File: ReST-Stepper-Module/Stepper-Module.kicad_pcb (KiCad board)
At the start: 2 copper layers, 46 x 32.8 mm, 16 parts, among them P1 CONN_02X10, P2 CONN_01X04, P3 CONN_01X04, P4 CONN_01X04, P5 CONN_01X04, P6 CONN_02X03, P7 CONN_02X03, U1 POLOLU_A4988, U2 POLOLU_A4988

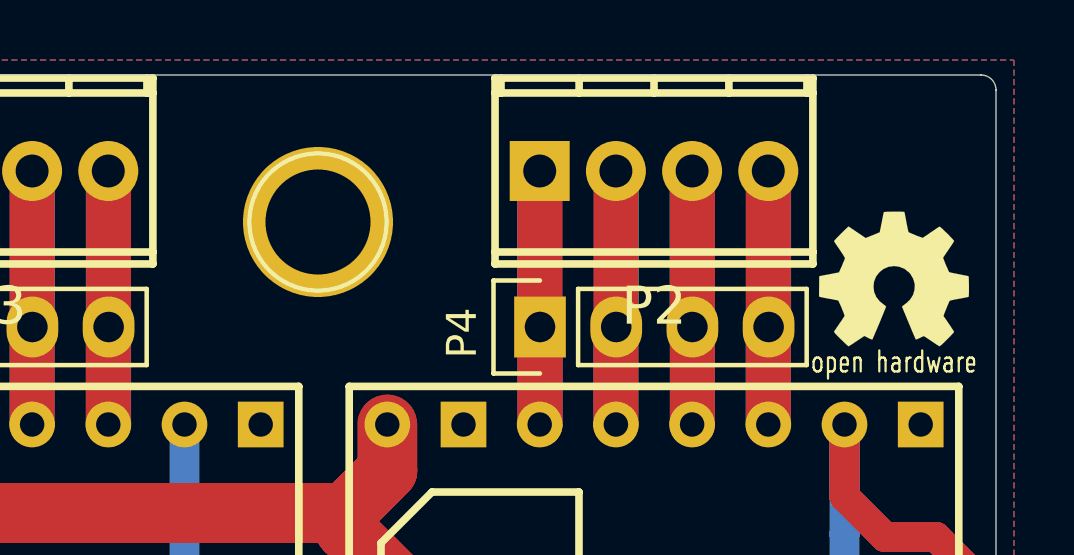
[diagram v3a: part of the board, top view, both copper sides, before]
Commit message: Added IRLML2502 Module and added Ground vias everywhere
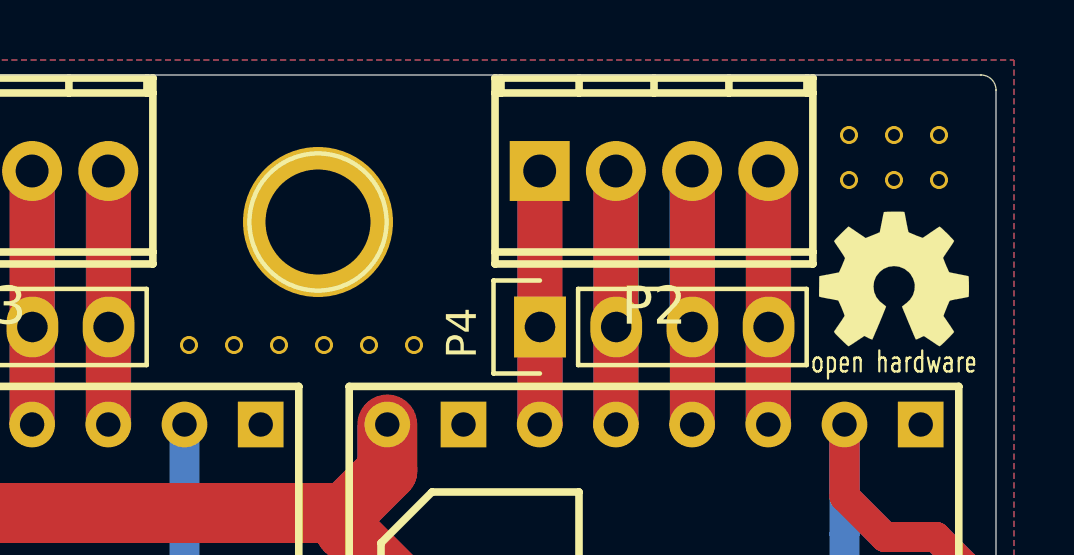
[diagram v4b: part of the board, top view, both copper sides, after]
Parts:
- added 11: , ReST-Library:VIA-0.6mm, F.Cu at (121.5, 87.0)
- added 21: , ReST-Library:VIA-0.6mm, F.Cu at (123.0, 87.0)
- added 31: , ReST-Library:VIA-0.6mm, F.Cu at (124.5, 87.0)
- added 41: , ReST-Library:VIA-0.6mm, F.Cu at (126.0, 87.0)
- added 51: , ReST-Library:VIA-0.6mm, F.Cu at (127.5, 87.0)
- added 61: , ReST-Library:VIA-0.6mm, F.Cu at (129.0, 87.0)
- added 611: , ReST-Library:VIA-0.6mm, F.Cu at (143.5, 80.0)
- added 612: , ReST-Library:VIA-0.6mm, F.Cu at (143.5, 81.5)
- added 621: , ReST-Library:VIA-0.6mm, F.Cu at (145.0, 80.0)
- added 622: , ReST-Library:VIA-0.6mm, F.Cu at (145.0, 81.5)
- added 631: , ReST-Library:VIA-0.6mm, F.Cu at (146.5, 80.0)
- added 632: , ReST-Library:VIA-0.6mm, F.Cu at (146.5, 81.5)
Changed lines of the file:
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@@
 (kicad_pcb (version 4) (host pcbnew 4.0.1-stable)
   (general
-    (links 63)
+    (links 75)
     (no_connects 0)
-    (area 84 59.2 165.800001 128.400001)
+    (area 102.394999 77.994999 148.405001 110.805001)
     (thickness 1.6)
     (drawings 9)
     (tracks 205)
     (zones 0)
-    (modules 16)
+    (modules 28)
     (nets 26)
   )
@@
     (mod_text_size 1 1)
     (mod_text_width 0.15)
-    (pad_size 5 5)
-    (pad_drill 3.5)
+    (pad_size 0.6 0.6)
+    (pad_drill 0.4)
     (pad_to_mask_clearance 0.2)
     (aux_axis_origin 0 0)
@@
     (add_net "Net-(U1-Pad13)")
     (add_net "Net-(U2-Pad13)")
+  )
+  (module ReST-Library:VIA-0.6mm (layer F.Cu)
+    (at 146.5 81.5)
+    (fp_text reference 632 (at 0 3.5) (layer F.SilkS) hide
+      (effects (font (size 1 1) (thickness 0.15)))
+    )
+    (fp_text value "" (at 0 -3) (layer F.Fab) hide
+      (effects (font (size 1 1) (thickness 0.15)))
+    )
+    (pad 2 thru_hole circle (at 0 0) (size 0.6 0.6) (drill 0.4) (layers *.Cu)
+      (net 2 GND) (zone_connect 2))
+  )
+  (module ReST-Library:VIA-0.6mm (layer F.Cu)
+    (at 145 81.5)
+    (fp_text reference 622 (at 0 3.5) (layer F.SilkS) hide
+      (effects (font (size 1 1) (thickness 0.15)))
+    )
+    (fp_text value "" (at 0 -3) (layer F.Fab) hide
+      (effects (font (size 1 1) (thickness 0.15)))
+    )
+    (pad 2 thru_hole circle (at 0 0) (size 0.6 0.6) (drill 0.4) (layers *.Cu)
+      (net 2 GND) (zone_connect 2))
+  )
+  (module ReST-Library:VIA-0.6mm (layer F.Cu)
+    (at 143.5 81.5)
+    (fp_text reference 612 (at 0 3.5) (layer F.SilkS) hide
+      (effects (font (size 1 1) (thickness 0.15)))
+    )
+    (fp_text value "" (at 0 -3) (layer F.Fab) hide
+      (effects (font (size 1 1) (thickness 0.15)))
+    )
+    (pad 2 thru_hole circle (at 0 0) (size 0.6 0.6) (drill 0.4) (layers *.Cu)
+      (net 2 GND) (zone_connect 2))
+  )
+  (module ReST-Library:VIA-0.6mm (layer F.Cu)
+    (at 146.5 80)
+    (fp_text reference 631 (at 0 3.5) (layer F.SilkS) hide
+      (effects (font (size 1 1) (thickness 0.15)))
+    )
+    (fp_text value "" (at 0 -3) (layer F.Fab) hide
+      (effects (font (size 1 1) (thickness 0.15)))
+    )
+    (pad 2 thru_hole circle (at 0 0) (size 0.6 0.6) (drill 0.4) (layers *.Cu)
+      (net 2 GND) (zone_connect 2))
+  )
+  (module ReST-Library:VIA-0.6mm (layer F.Cu)
+    (at 145 80)
+    (fp_text reference 621 (at 0 3.5) (layer F.SilkS) hide
+      (effects (font (size 1 1) (thickness 0.15)))
+    )
+    (fp_text value "" (at 0 -3) (layer F.Fab) hide
+      (effects (font (size 1 1) (thickness 0.15)))
+    )
+    (pad 2 thru_hole circle (at 0 0) (size 0.6 0.6) (drill 0.4) (layers *.Cu)
+      (net 2 GND) (zone_connect 2))
+  )
+  (module ReST-Library:VIA-0.6mm (layer F.Cu)
+    (at 143.5 80)
+    (fp_text reference 611 (at 0 3.5) (layer F.SilkS) hide
+      (effects (font (size 1 1) (thickness 0.15)))
+    )
+    (fp_text value "" (at 0 -3) (layer F.Fab) hide
+      (effects (font (size 1 1) (thickness 0.15)))
+    )
+    (pad 2 thru_hole circle (at 0 0) (size 0.6 0.6) (drill 0.4) (layers *.Cu)
+      (net 2 GND) (zone_connect 2))
+  )
+  (module ReST-Library:VIA-0.6mm (layer F.Cu)
+    (at 129 87)
+    (fp_text reference 61 (at 0 3.5) (layer F.SilkS) hide
+      (effects (font (size 1 1) (thickness 0.15)))
+    )
+    (fp_text value "" (at 0 -3) (layer F.Fab) hide
+      (effects (font (size 1 1) (thickness 0.15)))
+    )
+    (pad 2 thru_hole circle (at 0 0) (size 0.6 0.6) (drill 0.4) (layers *.Cu)
+      (net 2 GND) (zone_connect 2))
+  )
+  (module ReST-Library:VIA-0.6mm (layer F.Cu)
+    (at 127.5 87)
+    (fp_text reference 51 (at 0 3.5) (layer F.SilkS) hide
+      (effects (font (size 1 1) (thickness 0.15)))
+    )
+    (fp_text value "" (at 0 -3) (layer F.Fab) hide
+      (effects (font (size 1 1) (thickness 0.15)))
+    )
+    (pad 2 thru_hole circle (at 0 0) (size 0.6 0.6) (drill 0.4) (layers *.Cu)
+      (net 2 GND) (zone_connect 2))
+  )
+  (module ReST-Library:VIA-0.6mm (layer F.Cu)
+    (at 126 87)
+    (fp_text reference 41 (at 0 3.5) (layer F.SilkS) hide
+      (effects (font (size 1 1) (thickness 0.15)))
+    )
+    (fp_text value "" (at 0 -3) (layer F.Fab) hide
+      (effects (font (size 1 1) (thickness 0.15)))
+    )
+    (pad 2 thru_hole circle (at 0 0) (size 0.6 0.6) (drill 0.4) (layers *.Cu)
+      (net 2 GND) (zone_connect 2))
+  )
+  (module ReST-Library:VIA-0.6mm (layer F.Cu)
+    (at 124.5 87)
+    (fp_text reference 31 (at 0 3.5) (layer F.SilkS) hide
+      (effects (font (size 1 1) (thickness 0.15)))
+    )
+    (fp_text value "" (at 0 -3) (layer F.Fab) hide
+      (effects (font (size 1 1) (thickness 0.15)))
+    )
+    (pad 2 thru_hole circle (at 0 0) (size 0.6 0.6) (drill 0.4) (layers *.Cu)
+      (net 2 GND) (zone_connect 2))
+  )
+  (module ReST-Library:VIA-0.6mm (layer F.Cu)
+    (at 123 87)
+    (fp_text reference 21 (at 0 3.5) (layer F.SilkS) hide
+      (effects (font (size 1 1) (thickness 0.15)))
+    )
+    (fp_text value "" (at 0 -3) (layer F.Fab) hide
+      (effects (font (size 1 1) (thickness 0.15)))
+    )
+    (pad 2 thru_hole circle (at 0 0) (size 0.6 0.6) (drill 0.4) (layers *.Cu)
+      (net 2 GND) (zone_connect 2))
   )
   (module Pin_Headers:Pin_Header_Angled_2x10 (layer F.Cu)
@@
       (net 2 GND))
   )
+  (module ReST-Library:VIA-0.6mm (layer F.Cu)
+    (at 121.5 87)
+    (fp_text reference 11 (at 0 3.5) (layer F.SilkS) hide
+      (effects (font (size 1 1) (thickness 0.15)))
+    )
+    (fp_text value "" (at 0 -3) (layer F.Fab) hide
+      (effects (font (size 1 1) (thickness 0.15)))
+    )
+    (pad 2 thru_hole circle (at 0 0) (size 0.6 0.6) (drill 0.4) (layers *.Cu)
+      (net 2 GND) (zone_connect 2))
+  )
   (gr_arc (start 102.9 78.5) (end 102.4 78.5) (angle 90) (layer Edge.Cuts) (width 0.01))

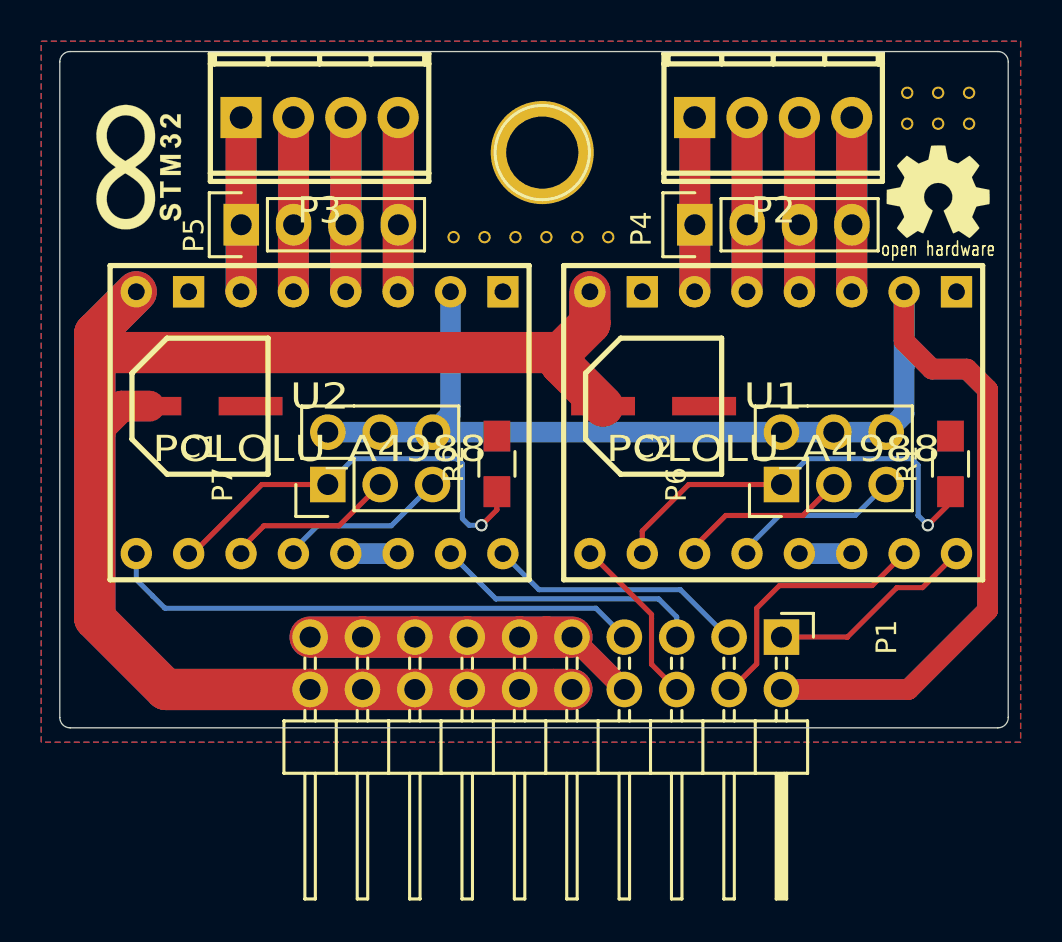
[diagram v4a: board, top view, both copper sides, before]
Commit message: Finished PCB design, notations and silkscreen
gonna work to finish a combined design for cheaper pcb cost and put
everything i need into the bom
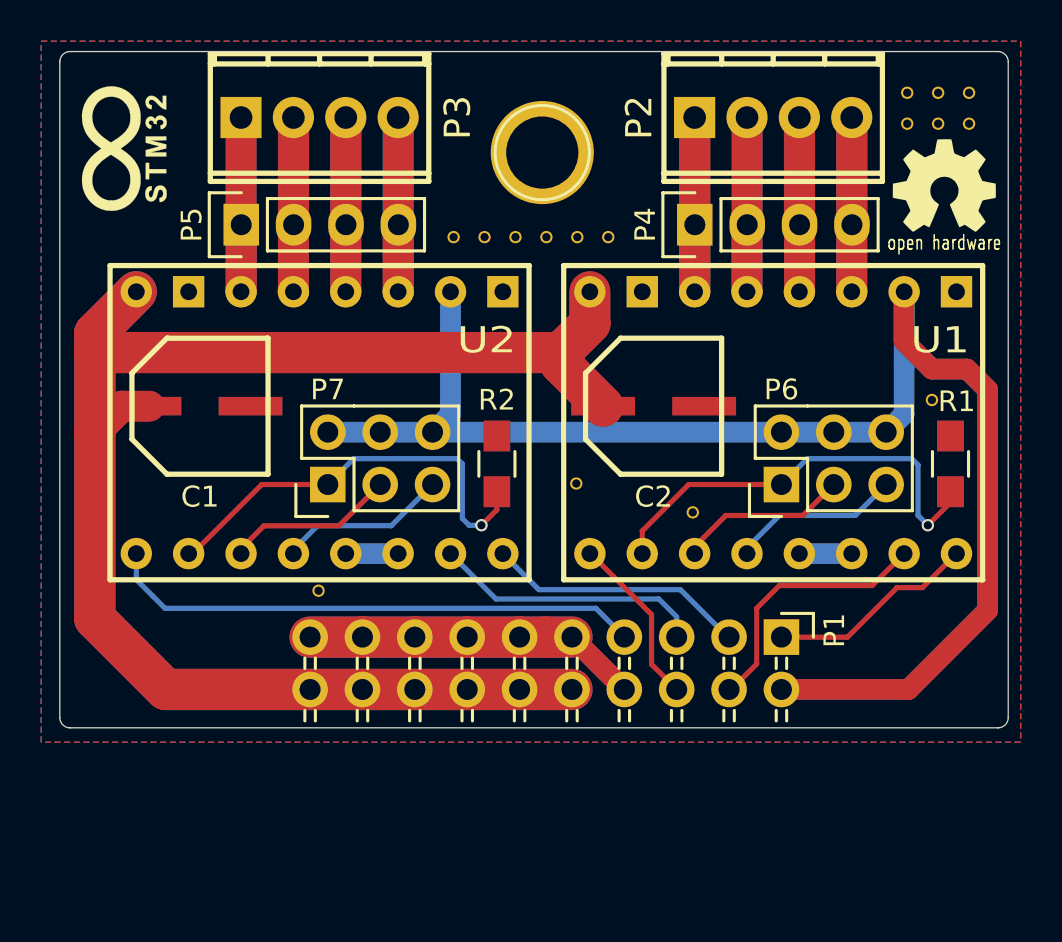
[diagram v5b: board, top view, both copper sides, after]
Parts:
- added ?: , ReST-Library:VIA-0.6mm, F.Cu at (144.7, 94.9)
- added ?: , ReST-Library:VIA-0.6mm, F.Cu at (133.1, 100.3)
- added ?: , ReST-Library:VIA-0.6mm, F.Cu at (115.0, 104.2)
- added ?: , ReST-Library:VIA-0.6mm, F.Cu at (127.5, 99.0)
- ? (x2): renamed from G***; value LOGO -> (none)
- ?: value 1pin -> (none)
- C1, C2: value 100uF -> (none)
- P1: value CONN_02X10 -> (none); footprint Pin_Headers:Pin_Header_Angled_2x10 -> ReST-Library:Pin_Header_Angled_2x10
- P2, P3, P4, P5: value CONN_01X04 -> (none)
- P6, P7: value CONN_02X03 -> (none)
- R1: value 100K -> (none)
- R2: value R_Small -> (none)
- U1, U2: value POLOLU_A4988 -> (none)
- moved ? 1.14 mm to (105.6, 82.7)
- moved ? 0.42 mm to (145.3, 84.5)
- renumbered 611 to ?, 61 to ?, 51 to ?, 41 to ?, 31 to ?, 21 to ?, 11 to ?, 632 to ?, 622 to ?, 612 to ?, 631 to ?, 621 to ?
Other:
- board text added: "ReST32 Stepper Module Rev. A @maker_berry"
- board text removed: "ReST32 Stepper Module Rev. A | Test by Straw"

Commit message: Final release
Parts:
- moved P2 0.15 mm to (137.0, 81.3)
- moved P3 0.15 mm to (115.0, 81.3)
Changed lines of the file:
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@@
     (links 79)
     (no_connects 0)
-    (area 102.394999 77.994999 148.405001 110.805001)
+    (area 100.8832 75.12512 149.000001 111.500001)
     (thickness 1.6)
     (drawings 9)
@@
     (visible_elements 7FFFFFFF)
     (pcbplotparams
-      (layerselection 0x00030_80000001)
-      (usegerberextensions false)
+      (layerselection 0x010f0_80000001)
+      (usegerberextensions true)
       (excludeedgelayer true)
       (linewidth 0.100000)
@@
       (outputformat 1)
       (mirror false)
-      (drillshape 1)
+      (drillshape 0)
       (scaleselection 1)
-      (outputdirectory ""))
+      (outputdirectory ../Gerber/Stepper/))
   )
   (net 0 "")
@@
   )
   (module 2:mpt_0,5%2f4-2,54 (layer F.Cu)
-    (at 137 81.2 180)
+    (at 137 81.35 180)
     (descr "4-way 2.54mm pitch terminal block, Phoenix MPT series")
     (fp_text reference P2 (at 6.5 0 270) (layer F.SilkS)
@@
   )
   (module 2:mpt_0,5%2f4-2,54 (layer F.Cu)
-    (at 115 81.2 180)
+    (at 115 81.35 180)
     (descr "4-way 2.54mm pitch terminal block, Phoenix MPT series")
     (fp_text reference P3 (at -6.7 0 270) (layer F.SilkS)
